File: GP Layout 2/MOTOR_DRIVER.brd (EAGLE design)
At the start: 91.4 x 97.5 mm, 91 parts, among them T1 2N2222, T2 2N2222, U7 ATMEGA328P_TQFP, Y1 16MHz

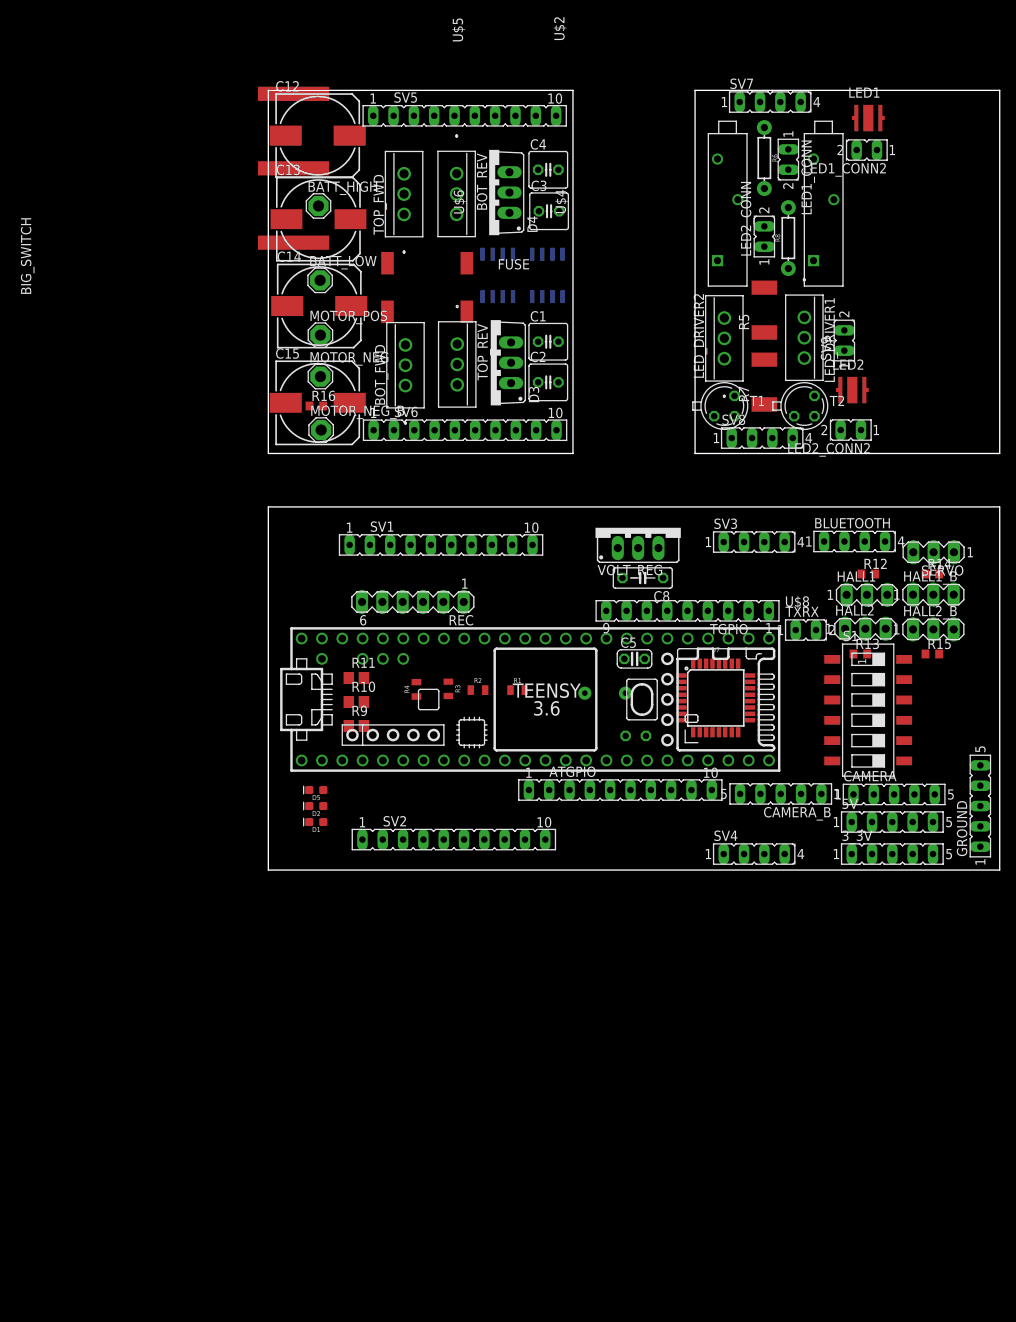
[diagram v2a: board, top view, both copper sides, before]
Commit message: modified placement
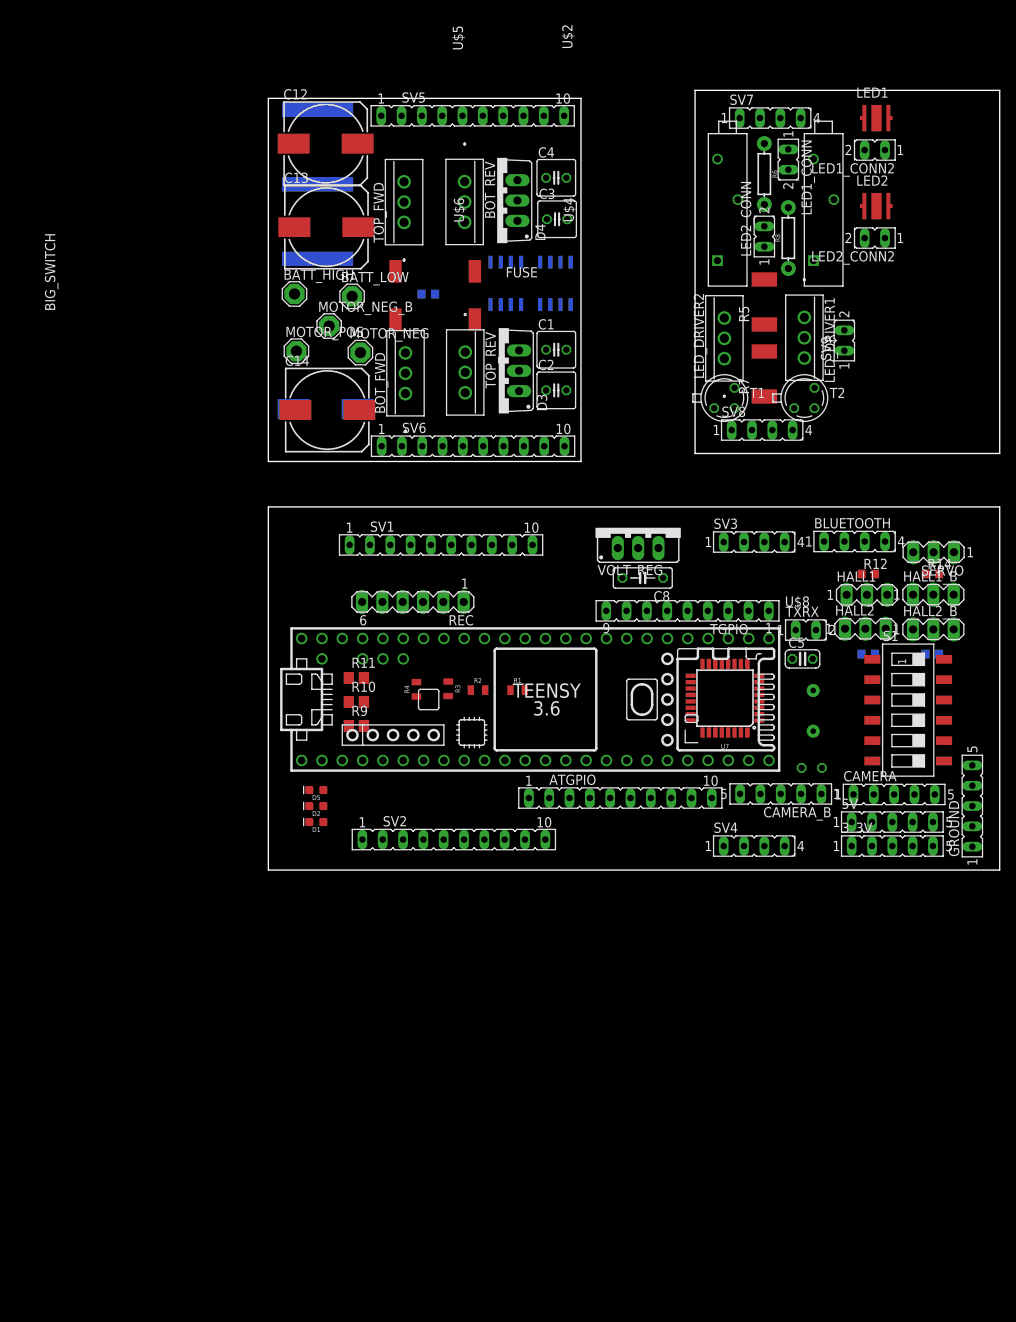
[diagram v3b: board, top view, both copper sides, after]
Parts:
- moved Y1 26.1 mm to (68.1, 19.9), turned to 90 degrees
- moved LED2_CONN2 24.2 mm to (72.0, 79.0)
- moved LED2 23.2 mm to (76.0, 83.0)
- moved C6 22.4 mm to (67.9, 12.8)
- moved C5 21.0 mm to (66.8, 26.4)
- moved R16 19.8 mm to (20.0, 72.0), flipped to the bottom, turned to 180 degrees
- moved C14 13.0 mm to (7.37, 57.5)
- moved MOTOR_NEG_B 13.0 mm to (7.60, 68.0)
- moved BATT_HIGH 11.4 mm to (3.27, 72.0)
- moved MOTOR_NEG 5.83 mm to (11.5, 64.7)
- moved S1 5.00 mm to (80.0, 20.0)
- moved BATT_LOW 4.47 mm to (10.5, 71.7)
- moved MOTOR_POS 3.61 mm to (3.51, 64.9)
- moved BIG_SWITCH 3.61 mm to (6.16, 81.1)
- moved SV6 2.24 mm to (25.6, 53.0)
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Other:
- outline, holes or cut-outs redrawn

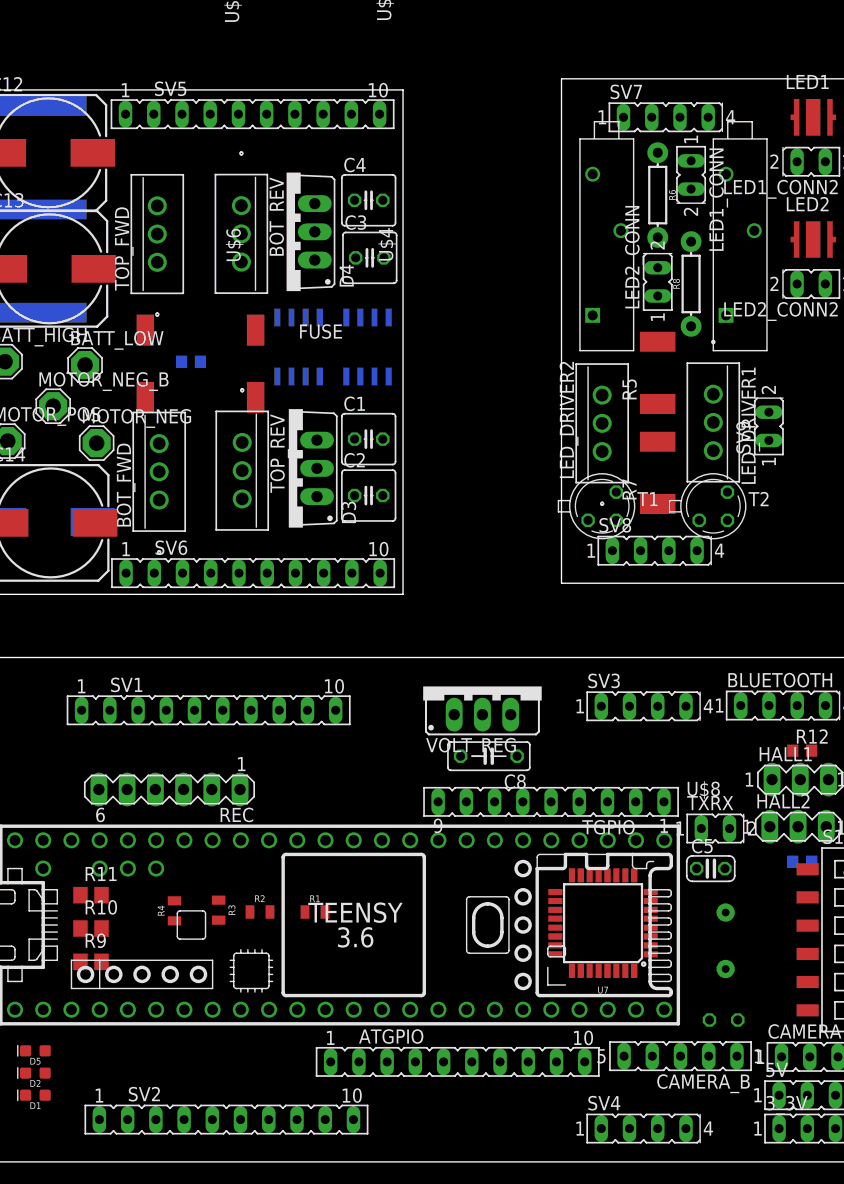
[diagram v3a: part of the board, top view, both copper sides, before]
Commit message: modified placement of header pins
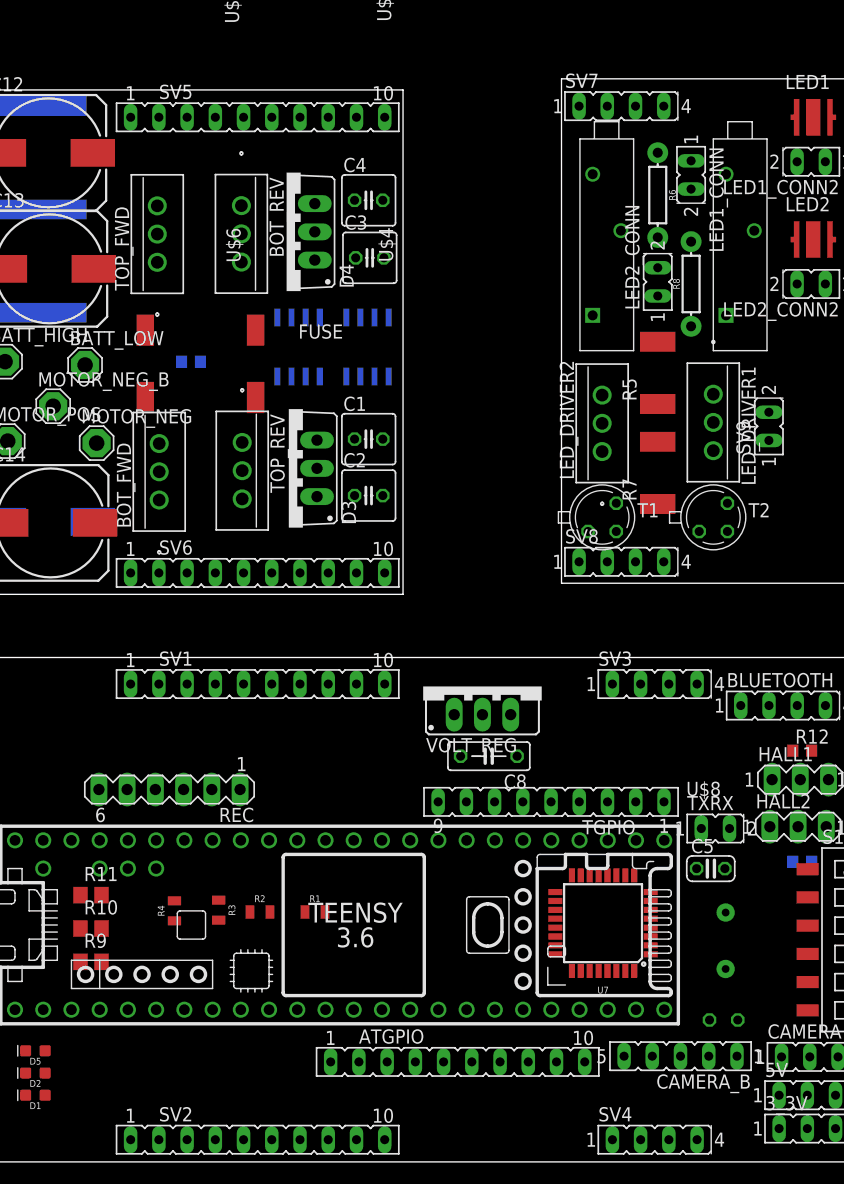
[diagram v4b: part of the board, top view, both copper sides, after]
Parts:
- moved SV1 5.00 mm to (26.0, 43.0)
- moved SV7 4.12 mm to (60.0, 95.0)
- moved SV2 3.34 mm to (26.0, 2.00)
- moved SV8 3.16 mm to (60.0, 54.0)
- moved SV3 2.24 mm to (63.0, 43.0)
- moved SV4 1.41 mm to (63.0, 2.00)
- moved T1 1.00 mm to (57.0, 58.0)
- moved T2 1.00 mm to (67.0, 58.0)
- moved SV5 0.54 mm to (26.0, 94.0)
- moved SV6 0.41 mm to (26.0, 53.0)
